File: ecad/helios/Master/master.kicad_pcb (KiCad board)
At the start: 2 copper layers, 100 x 100 mm, 129 parts, among them J1 MCV 1,5/ 3-G-3,5, J10 MiniFit JR 5556 08A2, J11 MCV 1,5/ 2-G-3,5, J12 MiniFit JR 5556 08A2, J13 M20-8760342, J2 MCV 1,5/ 2-G-3,5, J3 MCV 1,5/ 2-G-3,5, J4 MCV 1,5/ 2-G-3,5, J5 MCV 1,5/ 2-G-3,5, J6 MiniFit JR 5556 08A2, J7 MCV 1,5/ 2-G-3,5, J8 MiniFit JR 5556 08A2, J9 MCV 1,5/ 2-G-3,5, Q1 IRF9Z34NPbF, Q2 BSS84P, Q3 IRF9Z34NPbF, Q4 BSS84P, Q5 IRF9Z34NPbF, Q6 BSS84P, Q7 IRF9Z34NPbF, Q8 BSS84P, SW1 1825910-6, U1 NCP1117-5.0_SOT223, U10 ISO7320FC, U11 UA9638, U12 LM2842Y, U13 LP3985IM5-5.0/NOPB, U14 TPS1H100AQPWPRQ1, U15 ISO7320FC, U16 UA9638, U17 LM2842Y, U18 LP3985IM5-5.0/NOPB, U19 TPS1H100AQPWPRQ1, U2 MCP2561-E/SN, U20 ISO7320FC, U21 UA9638, U22 LM2842Y, U23 LP3985IM5-5.0/NOPB, U3 ATMEGA16M1-AU, U4 TPS1H100AQPWPRQ1, U5 ISO7320FC, U6 UA9638, U7 LM2842Y, U8 LP3985IM5-5.0/NOPB, U9 TPS1H100AQPWPRQ1, Y1 16MHz

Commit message: wip
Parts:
- added D14: 5.5V, FORT:D_0201, F.Cu at (127.5, 55.8)
- added D15: 5.5V, FORT:D_0201, F.Cu at (127.5, 54.2)
- added D16: 5.5V, FORT:D_0201, F.Cu at (127.5, 61.3)
- added D17: 5.5V, FORT:D_0201, F.Cu at (127.5, 59.7)
- added D18: 5.5V, FORT:D_0201, F.Cu at (177.5, 55.8)
- added D19: 5.5V, FORT:D_0201, F.Cu at (177.5, 54.2)
- added D20: 5.5V, FORT:D_0201, F.Cu at (177.5, 61.3)
- added D21: 5.5V, FORT:D_0201, F.Cu at (177.5, 59.7)
- added D22: 5.5V, FORT:D_0201, F.Cu at (152.5, 55.8)
- added D23: 5.5V, FORT:D_0201, F.Cu at (152.5, 54.2)
- added D24: 5.5V, FORT:D_0201, F.Cu at (152.5, 61.3)
- added D25: 5.5V, FORT:D_0201, F.Cu at (152.5, 59.7)
- added D26: 5.5V, FORT:D_0201, F.Cu at (102.5, 55.8)
- added D27: 5.5V, FORT:D_0201, F.Cu at (102.5, 54.2)
- added D28: 5.5V, FORT:D_0201, F.Cu at (102.7, 61.3)
- added D29: 5.5V, FORT:D_0201, F.Cu at (102.7, 59.7)
- added REF***: OSHW-Logo2_14.6x12mm_SilkScreen, Symbols:OSHW-Logo2_14.6x12mm_SilkScreen, F.Cu at (116.5, 129.8)
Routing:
- net /Output_3/PWRGND: track 344.8 -> 385.3 mm, vias 40 -> 45
- net /Output_1/PWRGND: track 360.4 -> 394.0 mm
- net /Output_4/PWRGND: track 349.1 -> 381.8 mm
- net +5V: track 291.4 -> 299.3 mm
- net (no net): track 6.00 -> 0.00 mm, vias 5 -> 0
- net /Output_3/DATA_-: track 62.3 -> 64.8 mm
- net /Output_1/IR_ON+: track 64.5 -> 66.2 mm
- net /Output_4/IR_ON+: track 64.5 -> 65.9 mm
- net /Output_3/IR_ON+: track 63.4 -> 64.8 mm
- net /Output_4/DATA_+: track 69.0 -> 70.4 mm
- net /Output_3/DATA_+: track 69.0 -> 70.4 mm
- net /Output_2/IR_ON+: track 63.7 -> 65.1 mm
- net /Output_1/IR_ON-: track 58.3 -> 59.6 mm
- net /Output_3/IR_ON-: track 57.7 -> 58.7 mm
- net /Output_4/IR_ON-: track 57.9 -> 59.0 mm
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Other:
- outline, holes or cut-outs redrawn
- net class Default: clearance 0.19 -> 0.175
- net class HighPower: clearance 0.19 -> 0.175
- net class LowPower: clearance 0.19 -> 0.175
- net class MidPower: clearance 0.19 -> 0.175
- rule trace_clearance: 0.19 -> 0.175
- board text added: "ICSP"
- board text added: "© 2018 Alexandre Tuleu HELIOS - Lighting Master Board"
- board text added: "•"

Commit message: wip
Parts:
- C13, C22, C31, C40: value 1uF -> 1uF, 50V
- C17, C26, C35, C44: value 0.01uF -> 10nF, 50V
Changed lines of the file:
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@@
     (pad_to_mask_clearance 0.08)
     (aux_axis_origin 102.5 128.7)
-    (grid_origin 100 150)
+    (grid_origin 102.5 128.7)
     (visible_elements FFFFFF7F)
     (pcbplotparams
@@
       (viasonmask false)
       (mode 1)
-      (useauxorigin false)
+      (useauxorigin true)
       (hpglpennumber 1)
       (hpglpenspeed 20)
@@
       (effects (font (size 1 1) (thickness 0.15)))
     )
-    (fp_text value 1uF (at 0 1.5 90) (layer F.Fab)
+    (fp_text value "1uF, 50V" (at 0 1.5 90) (layer F.Fab)
       (effects (font (size 1 1) (thickness 0.15)))
     )
@@
       (effects (font (size 1 1) (thickness 0.15)))
     )
-    (fp_text value 0.01uF (at 0 1.5 270) (layer F.Fab)
+    (fp_text value "10nF, 50V" (at 0 1.5 270) (layer F.Fab)
       (effects (font (size 1 1) (thickness 0.15)))
     )
@@
     (tags "capacitor 0603")
     (attr smd)
-    (fp_text reference C22 (at 0 -1.5 90) (layer F.SilkS)
+    (fp_text reference C22 (at 0 2.2 180) (layer F.SilkS)
       (effects (font (size 1 1) (thickness 0.15)))
     )
-    (fp_text value 1uF (at 0 1.5 90) (layer F.Fab)
+    (fp_text value "1uF, 50V" (at 0 1.5 90) (layer F.Fab)
       (effects (font (size 1 1) (thickness 0.15)))
     )
@@
     (tags "capacitor 1206")
     (attr smd)
-    (fp_text reference C24 (at 0 -1.75) (layer F.SilkS)
+    (fp_text reference C24 (at 3.6 0) (layer F.SilkS)
       (effects (font (size 1 1) (thickness 0.15)))
     )
@@
       (effects (font (size 1 1) (thickness 0.15)))
     )
-    (fp_text value 0.01uF (at 0 1.5 270) (layer F.Fab)
+    (fp_text value "10nF, 50V" (at 0 1.5 270) (layer F.Fab)
       (effects (font (size 1 1) (thickness 0.15)))
     )
@@
       (effects (font (size 1 1) (thickness 0.15)))
     )
-    (fp_text value 1uF (at 0 1.5 90) (layer F.Fab)
+    (fp_text value "1uF, 50V" (at 0 1.5 90) (layer F.Fab)
       (effects (font (size 1 1) (thickness 0.15)))
     )
@@
       (effects (font (size 1 1) (thickness 0.15)))
     )
-    (fp_text value 0.01uF (at 0 1.5 270) (layer F.Fab)
+    (fp_text value "10nF, 50V" (at 0 1.5 270) (layer F.Fab)
       (effects (font (size 1 1) (thickness 0.15)))
     )
@@
       (effects (font (size 1 1) (thickness 0.15)))
     )
-    (fp_text value 1uF (at 0 1.5 90) (layer F.Fab)
+    (fp_text value "1uF, 50V" (at 0 1.5 90) (layer F.Fab)
       (effects (font (size 1 1) (thickness 0.15)))
     )
@@
       (effects (font (size 1 1) (thickness 0.15)))
     )
-    (fp_text value 0.01uF (at 0 1.5 270) (layer F.Fab)
+    (fp_text value "10nF, 50V" (at 0 1.5 270) (layer F.Fab)
       (effects (font (size 1 1) (thickness 0.15)))
     )
@@
     (tags SOD-123)
     (attr smd)
-    (fp_text reference D6 (at 0 -2 90) (layer F.SilkS)
+    (fp_text reference D6 (at 2.9 0 180) (layer F.SilkS)
       (effects (font (size 1 1) (thickness 0.15)))
     )
@@
     (at 133.8 71.8 180)
     (attr smd)
-    (fp_text reference L1 (at -3.4 6.3 180) (layer F.SilkS)
+    (fp_text reference L1 (at 4.7 6.3 180) (layer F.SilkS)
       (effects (font (size 1 1) (thickness 0.15)))
     )
@@
     (at 108.8 71.8 180)
     (attr smd)
-    (fp_text reference L4 (at -3.4 6.3 180) (layer F.SilkS)
+    (fp_text reference L4 (at 4.7 6.3 180) (layer F.SilkS)
       (effects (font (size 1 1) (thickness 0.15)))
     )
@@
     (at 158.8 71.8 180)
     (attr smd)
-    (fp_text reference L3 (at -3.4 6.3 180) (layer F.SilkS)
+    (fp_text reference L3 (at 4.7 6.3 180) (layer F.SilkS)
       (effects (font (size 1 1) (thickness 0.15)))
     )
@@
     (at 183.8 71.8 180)
     (attr smd)
-    (fp_text reference L2 (at -3.4 6.3 180) (layer F.SilkS)
+    (fp_text reference L2 (at 4.7 6.4 180) (layer F.SilkS)
       (effects (font (size 1 1) (thickness 0.15)))
     )

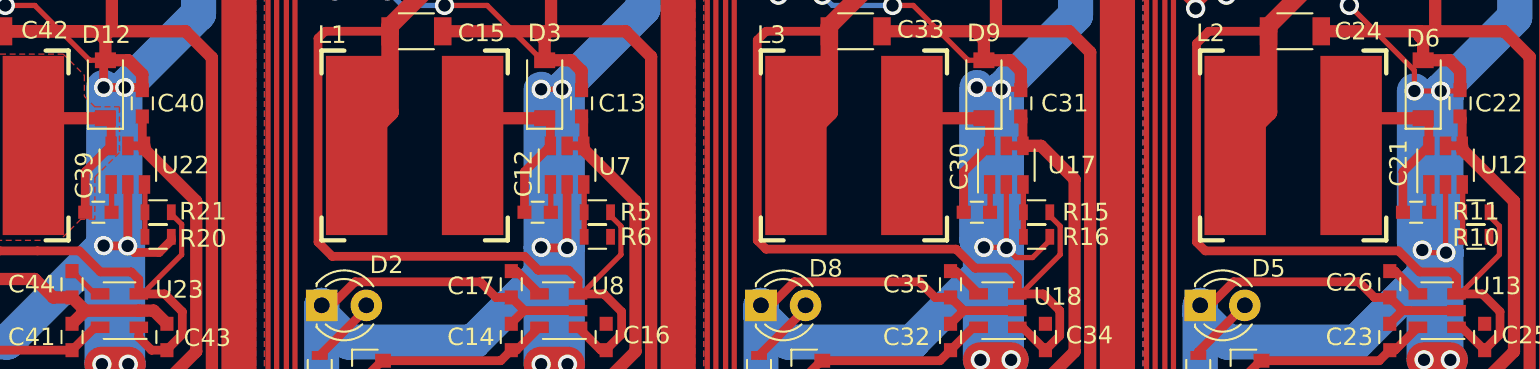
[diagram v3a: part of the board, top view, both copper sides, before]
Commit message: Adds step exports of all boards
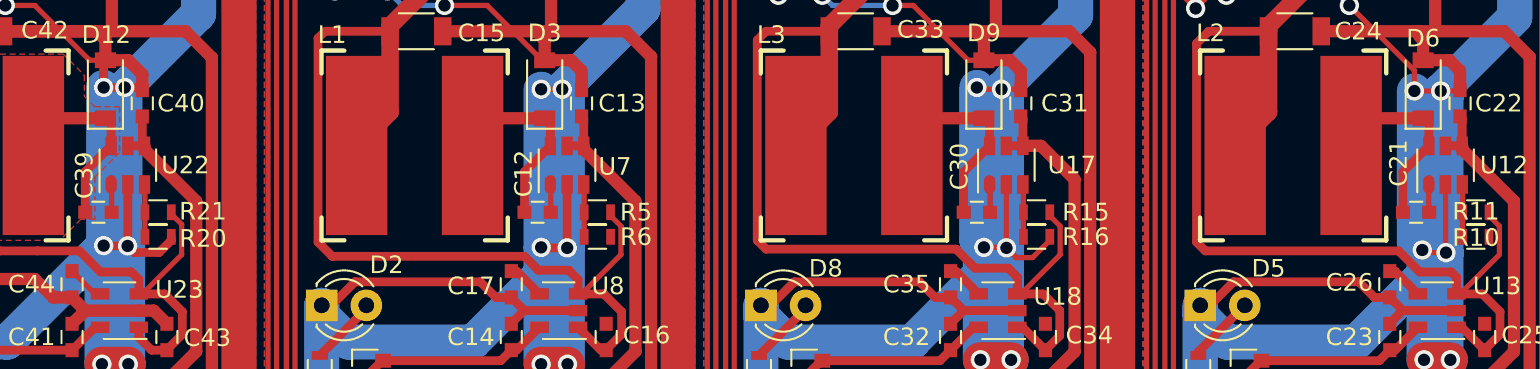
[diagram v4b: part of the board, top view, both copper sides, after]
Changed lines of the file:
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@@
     (links 394)
     (no_connects 0)
-    (area 98.55 49.924999 200.805952 150.075001)
+    (area 99.924999 49.924999 200.075001 150.075001)
     (thickness 1.6)
     (drawings 15)
@@
     (mod_text_size 1 1)
     (mod_text_width 0.15)
-    (pad_size 1.524 1.524)
-    (pad_drill 0.762)
+    (pad_size 1.06 0.65)
+    (pad_drill 0)
     (pad_to_mask_clearance 0.08)
     (aux_axis_origin 102.5 128.7)
@@
     (fp_line (start 0.9 1.55) (end -0.9 1.55) (layer F.Fab) (width 0.1))
     (fp_line (start 0.9 -1.55) (end 0.9 1.55) (layer F.Fab) (width 0.1))
-    (pad 1 smd rect (at -1.1 -0.95 90) (size 1.06 0.65) (layers F.Cu F.Paste F.Mask)
+    (pad 1 smd oval (at -1.1 -0.95 90) (size 1.06 0.65) (layers F.Cu F.Paste F.Mask)
       (net 45 /Output_2/6V_Regulator/BOOT))
     (pad 2 smd rect (at -1.1 0 90) (size 1.06 0.65) (layers F.Cu F.Paste F.Mask)
@@
     (fp_line (start 0.9 1.55) (end -0.9 1.55) (layer F.Fab) (width 0.1))
     (fp_line (start 0.9 -1.55) (end 0.9 1.55) (layer F.Fab) (width 0.1))
-    (pad 1 smd rect (at -1.1 -0.95 90) (size 1.06 0.65) (layers F.Cu F.Paste F.Mask)
+    (pad 1 smd oval (at -1.1 -0.95 90) (size 1.06 0.65) (layers F.Cu F.Paste F.Mask)
       (net 49 /Output_3/6V_Regulator/BOOT))
     (pad 2 smd rect (at -1.1 0 90) (size 1.06 0.65) (layers F.Cu F.Paste F.Mask)
@@
     (fp_line (start 0.9 1.55) (end -0.9 1.55) (layer F.Fab) (width 0.1))
     (fp_line (start 0.9 -1.55) (end 0.9 1.55) (layer F.Fab) (width 0.1))
-    (pad 1 smd rect (at -1.1 -0.95 90) (size 1.06 0.65) (layers F.Cu F.Paste F.Mask)
+    (pad 1 smd oval (at -1.1 -0.95 90) (size 1.06 0.65) (layers F.Cu F.Paste F.Mask)
       (net 53 /Output_4/6V_Regulator/BOOT))
     (pad 2 smd rect (at -1.1 0 90) (size 1.06 0.65) (layers F.Cu F.Paste F.Mask)
@@
     (fp_line (start 0.9 1.55) (end -0.9 1.55) (layer F.Fab) (width 0.1))
     (fp_line (start 0.9 -1.55) (end 0.9 1.55) (layer F.Fab) (width 0.1))
-    (pad 1 smd rect (at -1.1 -0.95 90) (size 1.06 0.65) (layers F.Cu F.Paste F.Mask)
+    (pad 1 smd oval (at -1.1 -0.95 90) (size 1.06 0.65) (layers F.Cu F.Paste F.Mask)
       (net 57 /Output_1/6V_Regulator/BOOT))
     (pad 2 smd rect (at -1.1 0 90) (size 1.06 0.65) (layers F.Cu F.Paste F.Mask)

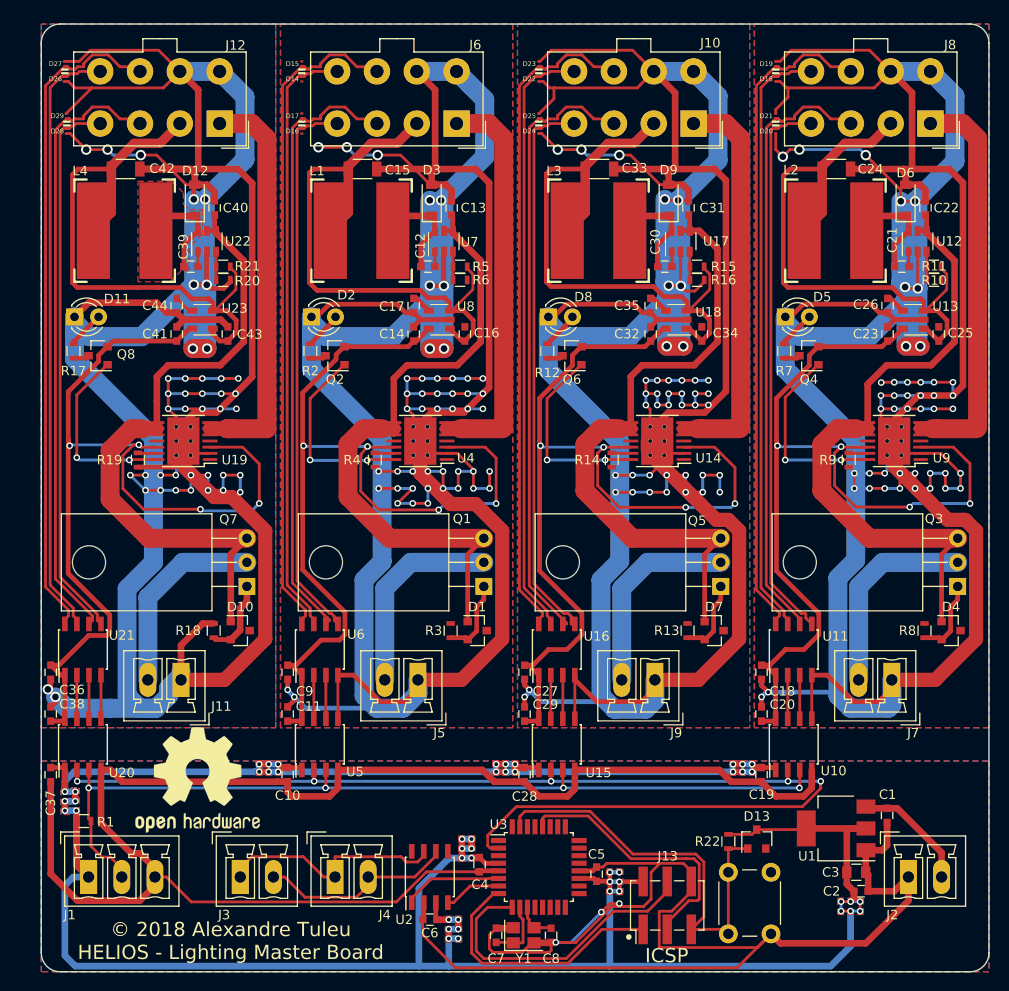
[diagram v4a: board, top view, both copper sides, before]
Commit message: Uses STEF01 instead of TPS1H100
The later makes everything explode on shortcut.

The former works nicely.
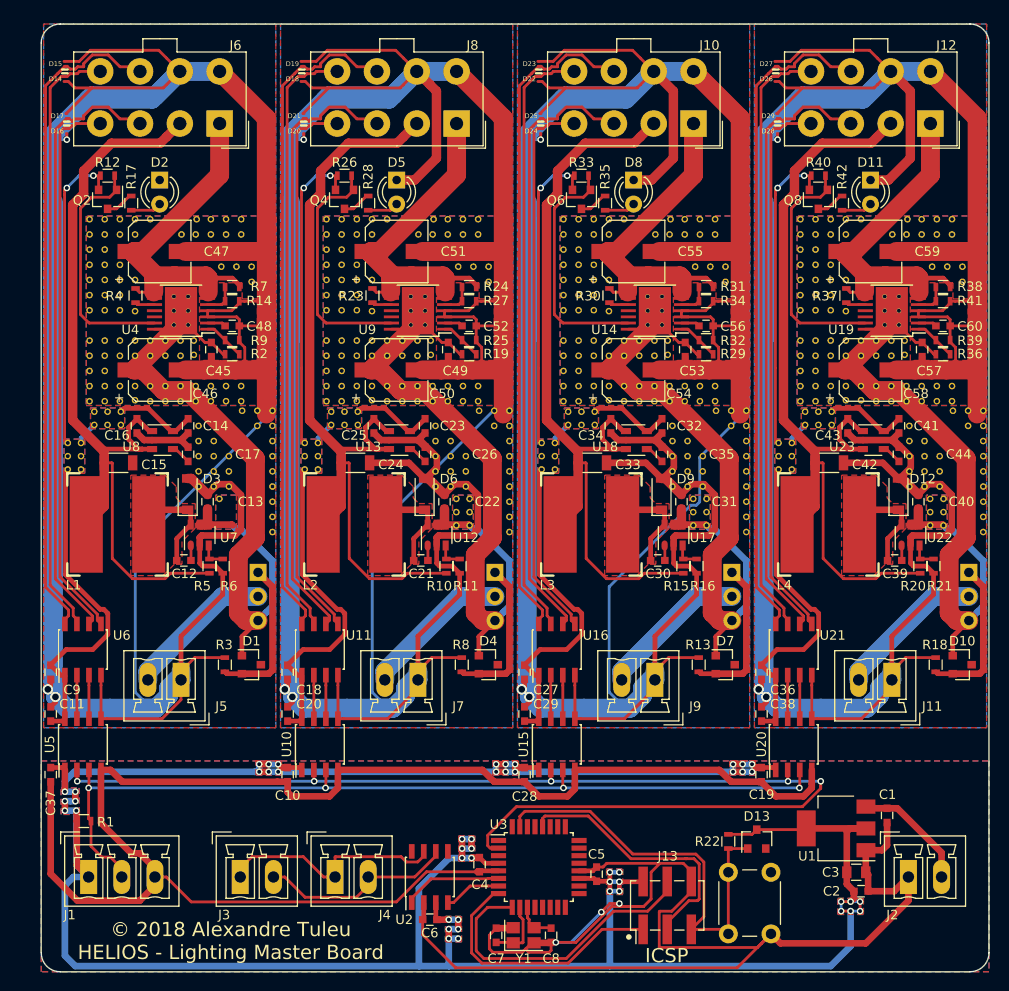
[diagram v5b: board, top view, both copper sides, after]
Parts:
- removed REF***: OSHW-Logo2_14.6x12mm_SilkScreen, Symbols:OSHW-Logo2_14.6x12mm_SilkScreen
- added C45: 100nF, Capacitors_SMD:C_0603, F.Cu at (118.0, 84.3)
- added C46: 47uF, 50V, Capacitors_SMD:CP_Elec_6.3x7.7, F.Cu at (112.5, 86.5)
- added C47: 47uF, 50V, Capacitors_SMD:CP_Elec_6.3x7.7, F.Cu at (112.5, 74.0)
- added C48: 10nF, 50V, Capacitors_SMD:C_0603, F.Cu at (120.2, 81.8)
- added C49: 100nF, Capacitors_SMD:C_0603, F.Cu at (142.9, 84.3)
- added C50: 47uF, 50V, Capacitors_SMD:CP_Elec_6.3x7.7, F.Cu at (137.5, 86.5)
- added C51: 47uF, 50V, Capacitors_SMD:CP_Elec_6.3x7.7, F.Cu at (137.5, 74.0)
- added C52: 10nF, 50V, Capacitors_SMD:C_0603, F.Cu at (145.2, 81.8)
- added C53: 100nF, Capacitors_SMD:C_0603, F.Cu at (167.9, 84.3)
- added C54: 47uF, 50V, Capacitors_SMD:CP_Elec_6.3x7.7, F.Cu at (162.5, 86.5)
- added C55: 47uF, 50V, Capacitors_SMD:CP_Elec_6.3x7.7, F.Cu at (162.5, 74.0)
- added C56: 10nF, 50V, Capacitors_SMD:C_0603, F.Cu at (170.2, 81.8)
- added C57: 100nF, Capacitors_SMD:C_0603, F.Cu at (192.9, 84.3)
- added C58: 47uF, 50V, Capacitors_SMD:CP_Elec_6.3x7.7, F.Cu at (187.5, 86.5)
- added C59: 47uF, 50V, Capacitors_SMD:CP_Elec_6.3x7.7, F.Cu at (187.5, 74.0)
- added C60: 10nF, 50V, Capacitors_SMD:C_0603, F.Cu at (195.2, 81.8)
- added R23: 25.5, Resistors_SMD:R_0603, F.Cu at (134.9, 78.7)
- added R24: 301K, Resistors_SMD:R_0603, F.Cu at (145.2, 77.8)
- added R25: 10K, Resistors_SMD:R_0603, F.Cu at (145.2, 83.3)
- added R26: 100K, Resistors_SMD:R_0603, F.Cu at (132.0, 66.0)
- added R27: 10K, Resistors_SMD:R_0603, F.Cu at (145.2, 79.2)
- added R28: 604, Resistors_SMD:R_0603, F.Cu at (134.5, 68.9)
- added R29: 249K, Resistors_SMD:R_0603, F.Cu at (170.2, 84.8)
- added R30: 25.5, Resistors_SMD:R_0603, F.Cu at (159.9, 78.7)
- added R31: 301K, Resistors_SMD:R_0603, F.Cu at (170.2, 77.8)
- added R32: 10K, Resistors_SMD:R_0603, F.Cu at (170.2, 83.3)
- added R33: 100K, Resistors_SMD:R_0603, F.Cu at (157.0, 66.0)
- added R34: 10K, Resistors_SMD:R_0603, F.Cu at (170.2, 79.2)
- added R35: 604, Resistors_SMD:R_0603, F.Cu at (159.5, 68.9)
- added R36: 249K, Resistors_SMD:R_0603, F.Cu at (195.2, 84.8)
- added R37: 25.5, Resistors_SMD:R_0603, F.Cu at (184.9, 78.7)
- added R38: 301K, Resistors_SMD:R_0603, F.Cu at (195.2, 77.8)
- added R39: 10K, Resistors_SMD:R_0603, F.Cu at (195.2, 83.3)
- added R40: 100K, Resistors_SMD:R_0603, F.Cu at (182.0, 66.0)
- added R41: 10K, Resistors_SMD:R_0603, F.Cu at (195.2, 79.2)
- added R42: 604, Resistors_SMD:R_0603, F.Cu at (184.5, 68.9)
- added REF**: VIA_0.7mm, VIA_0.7mm, F.Cu at (119.8, 98.8)
- added REF**: VIA_0.7mm, VIA_0.7mm, F.Cu at (118.2, 94.0)
- added REF**: VIA_0.7mm, VIA_0.7mm, F.Cu at (159.9, 88.2)
- added REF**: VIA_0.7mm, VIA_0.7mm, F.Cu at (158.3, 88.2)
- added REF**: VIA_0.7mm, VIA_0.7mm, F.Cu at (156.7, 88.2)
- added REF**: VIA_0.7mm, VIA_0.7mm, F.Cu at (121.1, 88.2)
- added REF**: VIA_0.7mm, VIA_0.7mm, F.Cu at (119.5, 88.2)
- added REF**: VIA_0.7mm, VIA_0.7mm, F.Cu at (117.9, 88.2)
- added REF**: VIA_0.7mm, VIA_0.7mm, F.Cu at (116.3, 88.2)
- added REF**: VIA_0.7mm, VIA_0.7mm, F.Cu at (114.7, 88.2)
- added REF**: VIA_0.7mm, VIA_0.7mm, F.Cu at (113.1, 88.2)
- added REF**: VIA_0.7mm, VIA_0.7mm, F.Cu at (111.5, 88.2)
- added REF**: VIA_0.7mm, VIA_0.7mm, F.Cu at (116.6, 94.0)
- added REF**: VIA_0.7mm, VIA_0.7mm, F.Cu at (109.9, 88.2)
- added REF**: VIA_0.7mm, VIA_0.7mm, F.Cu at (108.3, 88.2)
- added REF**: VIA_0.7mm, VIA_0.7mm, F.Cu at (106.7, 88.2)
- added REF**: VIA_0.7mm, VIA_0.7mm, F.Cu at (146.1, 89.8)
- added REF**: VIA_0.7mm, VIA_0.7mm, F.Cu at (144.5, 89.8)
- added REF**: VIA_0.7mm, VIA_0.7mm, F.Cu at (142.9, 89.8)
- added REF**: VIA_0.7mm, VIA_0.7mm, F.Cu at (141.3, 89.8)
- added REF**: VIA_0.7mm, VIA_0.7mm, F.Cu at (139.7, 89.8)
- added REF**: VIA_0.7mm, VIA_0.7mm, F.Cu at (138.1, 89.8)
- added REF**: VIA_0.7mm, VIA_0.7mm, F.Cu at (136.5, 89.8)
- added REF**: VIA_0.7mm, VIA_0.7mm, F.Cu at (169.8, 98.8)
- added REF**: VIA_0.7mm, VIA_0.7mm, F.Cu at (134.9, 89.7)
- added REF**: VIA_0.7mm, VIA_0.7mm, F.Cu at (133.3, 89.8)
- added REF**: VIA_0.7mm, VIA_0.7mm, F.Cu at (131.7, 89.8)
- added REF**: VIA_0.7mm, VIA_0.7mm, F.Cu at (146.1, 88.2)
- added REF**: VIA_0.7mm, VIA_0.7mm, F.Cu at (144.5, 88.2)
- added REF**: VIA_0.7mm, VIA_0.7mm, F.Cu at (142.9, 88.2)
- added REF**: VIA_0.7mm, VIA_0.7mm, F.Cu at (141.3, 88.2)
- added REF**: VIA_0.7mm, VIA_0.7mm, F.Cu at (139.7, 88.2)
- added REF**: VIA_0.7mm, VIA_0.7mm, F.Cu at (138.1, 88.2)
- added REF**: VIA_0.7mm, VIA_0.7mm, F.Cu at (136.5, 88.2)
- added REF**: VIA_0.7mm, VIA_0.7mm, F.Cu at (168.2, 98.8)
- added REF**: VIA_0.7mm, VIA_0.7mm, F.Cu at (134.9, 88.2)
- added REF**: VIA_0.7mm, VIA_0.7mm, F.Cu at (133.3, 88.2)
- added REF**: VIA_0.7mm, VIA_0.7mm, F.Cu at (131.7, 88.2)
- added REF**: VIA_0.7mm, VIA_0.7mm, F.Cu at (156.7, 86.6)
- added REF**: VIA_0.7mm, VIA_0.7mm, F.Cu at (106.7, 86.6)
- added REF**: VIA_0.7mm, VIA_0.7mm, F.Cu at (131.7, 86.6)
- added REF**: VIA_0.7mm, VIA_0.7mm, F.Cu at (141.1, 83.4)
- added REF**: VIA_0.7mm, VIA_0.7mm, F.Cu at (139.7, 83.4)
- added REF**: VIA_0.7mm, VIA_0.7mm, F.Cu at (138.1, 83.4)
- added REF**: VIA_0.7mm, VIA_0.7mm, F.Cu at (136.5, 83.4)
- added REF**: VIA_0.7mm, VIA_0.7mm, F.Cu at (166.6, 98.8)
- added REF**: VIA_0.7mm, VIA_0.7mm, F.Cu at (134.9, 83.4)
- added REF**: VIA_0.7mm, VIA_0.7mm, F.Cu at (133.3, 83.4)
- added REF**: VIA_0.7mm, VIA_0.7mm, F.Cu at (131.7, 83.4)
- added REF**: VIA_0.7mm, VIA_0.7mm, F.Cu at (116.1, 84.9)
- added REF**: VIA_0.7mm, VIA_0.7mm, F.Cu at (114.7, 85.0)
- added REF**: VIA_0.7mm, VIA_0.7mm, F.Cu at (113.1, 85.0)
- added REF**: VIA_0.7mm, VIA_0.7mm, F.Cu at (111.5, 85.0)
- added REF**: VIA_0.7mm, VIA_0.7mm, F.Cu at (109.9, 85.0)
- added REF**: VIA_0.7mm, VIA_0.7mm, F.Cu at (108.3, 85.0)
- added REF**: VIA_0.7mm, VIA_0.7mm, F.Cu at (106.7, 85.0)
- added REF**: VIA_0.7mm, VIA_0.7mm, F.Cu at (169.8, 97.2)
- added REF**: VIA_0.7mm, VIA_0.7mm, F.Cu at (166.1, 84.9)
- added REF**: VIA_0.7mm, VIA_0.7mm, F.Cu at (164.7, 85.0)
- added REF**: VIA_0.7mm, VIA_0.7mm, F.Cu at (163.1, 85.0)
- added REF**: VIA_0.7mm, VIA_0.7mm, F.Cu at (161.5, 85.0)
- added REF**: VIA_0.7mm, VIA_0.7mm, F.Cu at (159.9, 85.0)
- added REF**: VIA_0.7mm, VIA_0.7mm, F.Cu at (158.3, 85.0)
- added REF**: VIA_0.7mm, VIA_0.7mm, F.Cu at (156.7, 85.0)
- added REF**: VIA_0.7mm, VIA_0.7mm, F.Cu at (166.1, 83.4)
- added REF**: VIA_0.7mm, VIA_0.7mm, F.Cu at (164.7, 83.4)
- added REF**: VIA_0.7mm, VIA_0.7mm, F.Cu at (163.1, 83.4)
- added REF**: VIA_0.7mm, VIA_0.7mm, F.Cu at (168.2, 97.2)
- added REF**: VIA_0.7mm, VIA_0.7mm, F.Cu at (161.5, 83.4)
- added REF**: VIA_0.7mm, VIA_0.7mm, F.Cu at (159.9, 83.4)
- added REF**: VIA_0.7mm, VIA_0.7mm, F.Cu at (158.3, 83.4)
- added REF**: VIA_0.7mm, VIA_0.7mm, F.Cu at (156.7, 83.4)
- added REF**: VIA_0.7mm, VIA_0.7mm, F.Cu at (116.1, 83.4)
- added REF**: VIA_0.7mm, VIA_0.7mm, F.Cu at (114.7, 83.4)
- added REF**: VIA_0.7mm, VIA_0.7mm, F.Cu at (113.1, 83.4)
- added REF**: VIA_0.7mm, VIA_0.7mm, F.Cu at (111.5, 83.4)
- added REF**: VIA_0.7mm, VIA_0.7mm, F.Cu at (109.9, 83.4)
- added REF**: VIA_0.7mm, VIA_0.7mm, F.Cu at (108.3, 83.4)
- added REF**: VIA_0.7mm, VIA_0.7mm, F.Cu at (166.6, 97.2)
- added REF**: VIA_0.7mm, VIA_0.7mm, F.Cu at (106.7, 83.4)
- added REF**: VIA_0.7mm, VIA_0.7mm, F.Cu at (141.1, 84.9)
- added REF**: VIA_0.7mm, VIA_0.7mm, F.Cu at (139.7, 85.0)
- added REF**: VIA_0.7mm, VIA_0.7mm, F.Cu at (138.1, 85.0)
- added REF**: VIA_0.7mm, VIA_0.7mm, F.Cu at (136.5, 85.0)
- added REF**: VIA_0.7mm, VIA_0.7mm, F.Cu at (134.9, 85.0)
- added REF**: VIA_0.7mm, VIA_0.7mm, F.Cu at (133.3, 85.0)
- added REF**: VIA_0.7mm, VIA_0.7mm, F.Cu at (131.7, 85.0)
- added REF**: VIA_0.7mm, VIA_0.7mm, F.Cu at (155.1, 89.8)
- added REF**: VIA_0.7mm, VIA_0.7mm, F.Cu at (155.1, 88.2)
- added REF**: VIA_0.7mm, VIA_0.7mm, F.Cu at (169.8, 95.6)
- added REF**: VIA_0.7mm, VIA_0.7mm, F.Cu at (155.1, 86.6)
- added REF**: VIA_0.7mm, VIA_0.7mm, F.Cu at (155.1, 85.0)
- added REF**: VIA_0.7mm, VIA_0.7mm, F.Cu at (155.1, 83.4)
- added REF**: VIA_0.7mm, VIA_0.7mm, F.Cu at (130.1, 89.8)
- added REF**: VIA_0.7mm, VIA_0.7mm, F.Cu at (130.1, 88.2)
- added REF**: VIA_0.7mm, VIA_0.7mm, F.Cu at (130.1, 86.6)
- added REF**: VIA_0.7mm, VIA_0.7mm, F.Cu at (130.1, 85.0)
- added REF**: VIA_0.7mm, VIA_0.7mm, F.Cu at (130.1, 83.4)
- added REF**: VIA_0.7mm, VIA_0.7mm, F.Cu at (105.1, 89.8)
- added REF**: VIA_0.7mm, VIA_0.7mm, F.Cu at (105.1, 88.2)
- added REF**: VIA_0.7mm, VIA_0.7mm, F.Cu at (168.2, 95.6)
- added REF**: VIA_0.7mm, VIA_0.7mm, F.Cu at (105.1, 86.6)
- added REF**: VIA_0.7mm, VIA_0.7mm, F.Cu at (105.1, 85.0)
- added REF**: VIA_0.7mm, VIA_0.7mm, F.Cu at (105.1, 83.4)
- added REF**: VIA_0.7mm, VIA_0.7mm, F.Cu at (147.2, 77.2)
- added REF**: VIA_0.7mm, VIA_0.7mm, F.Cu at (147.2, 75.6)
- added REF**: VIA_0.7mm, VIA_0.7mm, F.Cu at (145.6, 75.6)
- added REF**: VIA_0.7mm, VIA_0.7mm, F.Cu at (172.2, 77.2)
- added REF**: VIA_0.7mm, VIA_0.7mm, F.Cu at (172.2, 75.6)
- added REF**: VIA_0.7mm, VIA_0.7mm, F.Cu at (170.6, 75.6)
- added REF**: VIA_0.7mm, VIA_0.7mm, F.Cu at (122.2, 77.2)
- added REF**: VIA_0.7mm, VIA_0.7mm, F.Cu at (118.2, 98.8)
- added REF**: VIA_0.7mm, VIA_0.7mm, F.Cu at (166.6, 95.6)
- added REF**: VIA_0.7mm, VIA_0.7mm, F.Cu at (122.2, 75.6)
- added REF**: VIA_0.7mm, VIA_0.7mm, F.Cu at (120.6, 75.6)
- added REF**: VIA_0.7mm, VIA_0.7mm, F.Cu at (197.2, 75.6)
- added REF**: VIA_0.7mm, VIA_0.7mm, F.Cu at (169.0, 75.6)
- added REF**: VIA_0.7mm, VIA_0.7mm, F.Cu at (144.0, 75.6)
- added REF**: VIA_0.7mm, VIA_0.7mm, F.Cu at (106.7, 73.8)
- added REF**: VIA_0.7mm, VIA_0.7mm, F.Cu at (131.7, 73.8)
- added REF**: VIA_0.7mm, VIA_0.7mm, F.Cu at (109.9, 77.0)
- added REF**: VIA_0.7mm, VIA_0.7mm, F.Cu at (108.3, 77.0)
- added REF**: VIA_0.7mm, VIA_0.7mm, F.Cu at (106.7, 77.0)
- added REF**: VIA_0.7mm, VIA_0.7mm, F.Cu at (168.2, 94.0)
- added REF**: VIA_0.7mm, VIA_0.7mm, F.Cu at (133.3, 78.6)
- added REF**: VIA_0.7mm, VIA_0.7mm, F.Cu at (131.7, 78.6)
- added REF**: VIA_0.7mm, VIA_0.7mm, F.Cu at (109.9, 80.3)
- added REF**: VIA_0.7mm, VIA_0.7mm, F.Cu at (108.3, 80.2)
- added REF**: VIA_0.7mm, VIA_0.7mm, F.Cu at (106.7, 80.2)
- added REF**: VIA_0.7mm, VIA_0.7mm, F.Cu at (158.3, 75.4)
- added REF**: VIA_0.7mm, VIA_0.7mm, F.Cu at (156.7, 75.4)
- added REF**: VIA_0.7mm, VIA_0.7mm, F.Cu at (133.3, 75.4)
- added REF**: VIA_0.7mm, VIA_0.7mm, F.Cu at (131.7, 75.4)
- added REF**: VIA_0.7mm, VIA_0.7mm, F.Cu at (134.9, 80.3)
- added REF**: VIA_0.7mm, VIA_0.7mm, F.Cu at (166.6, 94.0)
- added REF**: VIA_0.7mm, VIA_0.7mm, F.Cu at (133.3, 80.2)
- added REF**: VIA_0.7mm, VIA_0.7mm, F.Cu at (131.7, 80.2)
- added REF**: VIA_0.7mm, VIA_0.7mm, F.Cu at (159.9, 80.3)
- added REF**: VIA_0.7mm, VIA_0.7mm, F.Cu at (158.3, 80.2)
- added REF**: VIA_0.7mm, VIA_0.7mm, F.Cu at (156.7, 80.2)
- added REF**: VIA_0.7mm, VIA_0.7mm, F.Cu at (158.3, 78.6)
- added REF**: VIA_0.7mm, VIA_0.7mm, F.Cu at (156.7, 78.6)
- added REF**: VIA_0.7mm, VIA_0.7mm, F.Cu at (108.3, 78.6)
- added REF**: VIA_0.7mm, VIA_0.7mm, F.Cu at (106.7, 78.6)
- added REF**: VIA_0.7mm, VIA_0.7mm, F.Cu at (108.3, 75.4)
- added REF**: VIA_0.7mm, VIA_0.7mm, F.Cu at (144.8, 98.8)
- added REF**: VIA_0.7mm, VIA_0.7mm, F.Cu at (106.7, 75.4)
- added REF**: VIA_0.7mm, VIA_0.7mm, F.Cu at (134.9, 77.0)
- added REF**: VIA_0.7mm, VIA_0.7mm, F.Cu at (133.3, 77.0)
- added REF**: VIA_0.7mm, VIA_0.7mm, F.Cu at (131.7, 77.0)
- added REF**: VIA_0.7mm, VIA_0.7mm, F.Cu at (159.9, 77.0)
- added REF**: VIA_0.7mm, VIA_0.7mm, F.Cu at (158.3, 77.0)
- added REF**: VIA_0.7mm, VIA_0.7mm, F.Cu at (156.7, 77.0)
- added REF**: VIA_0.7mm, VIA_0.7mm, F.Cu at (156.7, 73.8)
- added REF**: VIA_0.7mm, VIA_0.7mm, F.Cu at (146.1, 72.2)
- added REF**: VIA_0.7mm, VIA_0.7mm, F.Cu at (144.5, 72.2)
- added REF**: VIA_0.7mm, VIA_0.7mm, F.Cu at (143.2, 98.8)
- added REF**: VIA_0.7mm, VIA_0.7mm, F.Cu at (142.9, 72.2)
- added REF**: VIA_0.7mm, VIA_0.7mm, F.Cu at (141.3, 72.2)
- added REF**: VIA_0.7mm, VIA_0.7mm, F.Cu at (139.8, 72.2)
- added REF**: VIA_0.7mm, VIA_0.7mm, F.Cu at (134.9, 72.2)
- added REF**: VIA_0.7mm, VIA_0.7mm, F.Cu at (133.3, 72.2)
- added REF**: VIA_0.7mm, VIA_0.7mm, F.Cu at (131.7, 72.2)
- added REF**: VIA_0.7mm, VIA_0.7mm, F.Cu at (146.1, 70.6)
- added REF**: VIA_0.7mm, VIA_0.7mm, F.Cu at (144.5, 70.6)
- added REF**: VIA_0.7mm, VIA_0.7mm, F.Cu at (142.9, 70.6)
- added REF**: VIA_0.7mm, VIA_0.7mm, F.Cu at (141.4, 70.6)
- added REF**: VIA_0.7mm, VIA_0.7mm, F.Cu at (141.6, 98.8)
- added REF**: VIA_0.7mm, VIA_0.7mm, F.Cu at (136.5, 70.6)
- added REF**: VIA_0.7mm, VIA_0.7mm, F.Cu at (134.9, 70.6)
- added REF**: VIA_0.7mm, VIA_0.7mm, F.Cu at (133.3, 70.6)
- added REF**: VIA_0.7mm, VIA_0.7mm, F.Cu at (131.7, 70.6)
- added REF**: VIA_0.7mm, VIA_0.7mm, F.Cu at (121.1, 72.2)
- added REF**: VIA_0.7mm, VIA_0.7mm, F.Cu at (119.5, 72.2)
- added REF**: VIA_0.7mm, VIA_0.7mm, F.Cu at (117.9, 72.2)
- added REF**: VIA_0.7mm, VIA_0.7mm, F.Cu at (116.3, 72.2)
- added REF**: VIA_0.7mm, VIA_0.7mm, F.Cu at (114.8, 72.2)
- added REF**: VIA_0.7mm, VIA_0.7mm, F.Cu at (109.9, 72.2)
- added REF**: VIA_0.7mm, VIA_0.7mm, F.Cu at (144.8, 97.2)
- added REF**: VIA_0.7mm, VIA_0.7mm, F.Cu at (108.3, 72.2)
- added REF**: VIA_0.7mm, VIA_0.7mm, F.Cu at (106.7, 72.2)
- added REF**: VIA_0.7mm, VIA_0.7mm, F.Cu at (121.1, 70.6)
- added REF**: VIA_0.7mm, VIA_0.7mm, F.Cu at (119.5, 70.6)
- added REF**: VIA_0.7mm, VIA_0.7mm, F.Cu at (117.9, 70.6)
- added REF**: VIA_0.7mm, VIA_0.7mm, F.Cu at (116.4, 70.6)
- added REF**: VIA_0.7mm, VIA_0.7mm, F.Cu at (111.5, 70.6)
- added REF**: VIA_0.7mm, VIA_0.7mm, F.Cu at (109.9, 70.6)
- added REF**: VIA_0.7mm, VIA_0.7mm, F.Cu at (108.3, 70.6)
- added REF**: VIA_0.7mm, VIA_0.7mm, F.Cu at (106.7, 70.6)
- added REF**: VIA_0.7mm, VIA_0.7mm, F.Cu at (143.2, 97.2)
- added REF**: VIA_0.7mm, VIA_0.7mm, F.Cu at (155.1, 72.2)
- added REF**: VIA_0.7mm, VIA_0.7mm, F.Cu at (155.1, 70.6)
- added REF**: VIA_0.7mm, VIA_0.7mm, F.Cu at (171.1, 70.6)
- added REF**: VIA_0.7mm, VIA_0.7mm, F.Cu at (169.5, 70.6)
- added REF**: VIA_0.7mm, VIA_0.7mm, F.Cu at (167.9, 70.6)
- added REF**: VIA_0.7mm, VIA_0.7mm, F.Cu at (166.4, 70.6)
- added REF**: VIA_0.7mm, VIA_0.7mm, F.Cu at (161.5, 70.6)
- added REF**: VIA_0.7mm, VIA_0.7mm, F.Cu at (159.9, 70.6)
- added REF**: VIA_0.7mm, VIA_0.7mm, F.Cu at (158.3, 70.6)
- added REF**: VIA_0.7mm, VIA_0.7mm, F.Cu at (156.7, 70.6)
- added REF**: VIA_0.7mm, VIA_0.7mm, F.Cu at (141.6, 97.2)
- added REF**: VIA_0.7mm, VIA_0.7mm, F.Cu at (171.1, 72.2)
- added REF**: VIA_0.7mm, VIA_0.7mm, F.Cu at (169.5, 72.2)
- added REF**: VIA_0.7mm, VIA_0.7mm, F.Cu at (167.9, 72.2)
- added REF**: VIA_0.7mm, VIA_0.7mm, F.Cu at (166.3, 72.2)
- added REF**: VIA_0.7mm, VIA_0.7mm, F.Cu at (164.8, 72.2)
- added REF**: VIA_0.7mm, VIA_0.7mm, F.Cu at (159.9, 72.2)
- added REF**: VIA_0.7mm, VIA_0.7mm, F.Cu at (158.3, 72.2)
- added REF**: VIA_0.7mm, VIA_0.7mm, F.Cu at (156.7, 72.2)
- added REF**: VIA_0.7mm, VIA_0.7mm, F.Cu at (130.1, 80.2)
- added REF**: VIA_0.7mm, VIA_0.7mm, F.Cu at (130.1, 78.6)
- added REF**: VIA_0.7mm, VIA_0.7mm, F.Cu at (144.8, 95.6)
- added REF**: VIA_0.7mm, VIA_0.7mm, F.Cu at (130.1, 77.0)
- added REF**: VIA_0.7mm, VIA_0.7mm, F.Cu at (130.1, 75.4)
- added REF**: VIA_0.7mm, VIA_0.7mm, F.Cu at (130.1, 73.8)
- added REF**: VIA_0.7mm, VIA_0.7mm, F.Cu at (130.1, 72.2)
- added REF**: VIA_0.7mm, VIA_0.7mm, F.Cu at (155.1, 80.2)
- added REF**: VIA_0.7mm, VIA_0.7mm, F.Cu at (155.1, 78.6)
- added REF**: VIA_0.7mm, VIA_0.7mm, F.Cu at (155.1, 77.0)
- added REF**: VIA_0.7mm, VIA_0.7mm, F.Cu at (155.1, 75.4)
- added REF**: VIA_0.7mm, VIA_0.7mm, F.Cu at (155.1, 73.8)
- added REF**: VIA_0.7mm, VIA_0.7mm, F.Cu at (105.1, 80.2)
- added REF**: VIA_0.7mm, VIA_0.7mm, F.Cu at (116.6, 98.8)
- added REF**: VIA_0.7mm, VIA_0.7mm, F.Cu at (143.2, 95.6)
- added REF**: VIA_0.7mm, VIA_0.7mm, F.Cu at (105.1, 78.6)
- added REF**: VIA_0.7mm, VIA_0.7mm, F.Cu at (105.1, 77.0)
- added REF**: VIA_0.7mm, VIA_0.7mm, F.Cu at (105.1, 75.4)
- added REF**: VIA_0.7mm, VIA_0.7mm, F.Cu at (105.1, 73.8)
- added REF**: VIA_0.7mm, VIA_0.7mm, F.Cu at (105.1, 72.2)
- added REF**: VIA_0.7mm, VIA_0.7mm, F.Cu at (158.4, 92.3)
- added REF**: VIA_0.7mm, VIA_0.7mm, F.Cu at (157.0, 92.3)
- added REF**: VIA_0.7mm, VIA_0.7mm, F.Cu at (155.6, 92.3)
- added REF**: VIA_0.7mm, VIA_0.7mm, F.Cu at (158.4, 90.9)
- added REF**: VIA_0.7mm, VIA_0.7mm, F.Cu at (157.0, 90.9)
- added REF**: VIA_0.7mm, VIA_0.7mm, F.Cu at (141.6, 95.6)
- added REF**: VIA_0.7mm, VIA_0.7mm, F.Cu at (170.2, 102.9)
- added REF**: VIA_0.7mm, VIA_0.7mm, F.Cu at (168.8, 102.9)
- added REF**: VIA_0.7mm, VIA_0.7mm, F.Cu at (170.2, 101.5)
- added REF**: VIA_0.7mm, VIA_0.7mm, F.Cu at (168.8, 101.5)
- added REF**: VIA_0.7mm, VIA_0.7mm, F.Cu at (170.2, 100.1)
- added REF**: VIA_0.7mm, VIA_0.7mm, F.Cu at (154.2, 97.0)
- added REF**: VIA_0.7mm, VIA_0.7mm, F.Cu at (152.8, 97.0)
- added REF**: VIA_0.7mm, VIA_0.7mm, F.Cu at (154.2, 95.6)
- added REF**: VIA_0.7mm, VIA_0.7mm, F.Cu at (152.8, 95.6)
- added REF**: VIA_0.7mm, VIA_0.7mm, F.Cu at (154.2, 94.2)
- added REF**: VIA_0.7mm, VIA_0.7mm, F.Cu at (143.2, 94.0)
- added REF**: VIA_0.7mm, VIA_0.7mm, F.Cu at (145.2, 102.9)
- added REF**: VIA_0.7mm, VIA_0.7mm, F.Cu at (143.8, 102.9)
- added REF**: VIA_0.7mm, VIA_0.7mm, F.Cu at (145.2, 101.5)
- added REF**: VIA_0.7mm, VIA_0.7mm, F.Cu at (143.8, 101.5)
- added REF**: VIA_0.7mm, VIA_0.7mm, F.Cu at (145.2, 100.1)
- added REF**: VIA_0.7mm, VIA_0.7mm, F.Cu at (129.2, 97.0)
- added REF**: VIA_0.7mm, VIA_0.7mm, F.Cu at (127.8, 97.0)
- added REF**: VIA_0.7mm, VIA_0.7mm, F.Cu at (129.2, 95.6)
- added REF**: VIA_0.7mm, VIA_0.7mm, F.Cu at (127.8, 95.6)
- added REF**: VIA_0.7mm, VIA_0.7mm, F.Cu at (129.2, 94.2)
- added REF**: VIA_0.7mm, VIA_0.7mm, F.Cu at (141.6, 94.0)
- added REF**: VIA_0.7mm, VIA_0.7mm, F.Cu at (133.4, 92.3)
- added REF**: VIA_0.7mm, VIA_0.7mm, F.Cu at (132.0, 92.3)
- added REF**: VIA_0.7mm, VIA_0.7mm, F.Cu at (130.6, 92.3)
- added REF**: VIA_0.7mm, VIA_0.7mm, F.Cu at (133.4, 90.9)
- added REF**: VIA_0.7mm, VIA_0.7mm, F.Cu at (132.0, 90.9)
- added REF**: VIA_0.7mm, VIA_0.7mm, F.Cu at (104.2, 97.0)
- added REF**: VIA_0.7mm, VIA_0.7mm, F.Cu at (102.8, 97.0)
- added REF**: VIA_0.7mm, VIA_0.7mm, F.Cu at (104.2, 95.6)
- added REF**: VIA_0.7mm, VIA_0.7mm, F.Cu at (102.8, 95.6)
- added REF**: VIA_0.7mm, VIA_0.7mm, F.Cu at (104.2, 94.2)
- added REF**: VIA_0.7mm, VIA_0.7mm, F.Cu at (191.6, 92.4)
- added REF**: VIA_0.7mm, VIA_0.7mm, F.Cu at (108.4, 92.3)
- added REF**: VIA_0.7mm, VIA_0.7mm, F.Cu at (107.0, 92.3)
- added REF**: VIA_0.7mm, VIA_0.7mm, F.Cu at (105.6, 92.3)
- added REF**: VIA_0.7mm, VIA_0.7mm, F.Cu at (108.4, 90.9)
- added REF**: VIA_0.7mm, VIA_0.7mm, F.Cu at (107.0, 90.9)
- added REF**: VIA_0.7mm, VIA_0.7mm, F.Cu at (155.6, 90.9)
- added REF**: VIA_0.7mm, VIA_0.7mm, F.Cu at (130.6, 90.9)
- added REF**: VIA_0.7mm, VIA_0.7mm, F.Cu at (105.6, 90.9)
- added REF**: VIA_0.7mm, VIA_0.7mm, F.Cu at (152.8, 94.2)
- added REF**: VIA_0.7mm, VIA_0.7mm, F.Cu at (127.8, 94.2)
- added REF**: VIA_0.7mm, VIA_0.7mm, F.Cu at (166.6, 92.4)
- added REF**: VIA_0.7mm, VIA_0.7mm, F.Cu at (102.8, 94.2)
- added REF**: VIA_0.7mm, VIA_0.7mm, F.Cu at (130.1, 70.6)
- added REF**: VIA_0.7mm, VIA_0.7mm, F.Cu at (105.1, 70.6)
- added REF**: VIA_0.7mm, VIA_0.7mm, F.Cu at (168.8, 100.1)
- added REF**: VIA_0.7mm, VIA_0.7mm, F.Cu at (143.8, 100.1)
- added REF**: VIA_0.7mm, VIA_0.7mm, F.Cu at (118.8, 100.1)
- added REF**: VIA_0.7mm, VIA_0.7mm, F.Cu at (171.2, 90.8)
- added REF**: VIA_0.7mm, VIA_0.7mm, F.Cu at (146.2, 90.8)
- added REF**: VIA_0.7mm, VIA_0.7mm, F.Cu at (121.2, 90.8)
- added REF**: VIA_0.7mm, VIA_0.7mm, F.Cu at (199.4, 98.8)
- added REF**: VIA_0.7mm, VIA_0.7mm, F.Cu at (141.6, 92.4)
- added REF**: VIA_0.7mm, VIA_0.7mm, F.Cu at (194.8, 98.8)
- added REF**: VIA_0.7mm, VIA_0.7mm, F.Cu at (193.2, 98.8)
- added REF**: VIA_0.7mm, VIA_0.7mm, F.Cu at (191.6, 98.8)
- added REF**: VIA_0.7mm, VIA_0.7mm, F.Cu at (199.4, 97.2)
- added REF**: VIA_0.7mm, VIA_0.7mm, F.Cu at (194.8, 97.2)
- added REF**: VIA_0.7mm, VIA_0.7mm, F.Cu at (193.2, 97.2)
- added REF**: VIA_0.7mm, VIA_0.7mm, F.Cu at (191.6, 97.2)
- added REF**: VIA_0.7mm, VIA_0.7mm, F.Cu at (199.4, 95.6)
- added REF**: VIA_0.7mm, VIA_0.7mm, F.Cu at (194.8, 95.6)
- added REF**: VIA_0.7mm, VIA_0.7mm, F.Cu at (193.2, 95.6)
- added REF**: VIA_0.7mm, VIA_0.7mm, F.Cu at (124.4, 103.6)
- added REF**: VIA_0.7mm, VIA_0.7mm, F.Cu at (191.6, 95.6)
- added REF**: VIA_0.7mm, VIA_0.7mm, F.Cu at (199.4, 94.0)
- added REF**: VIA_0.7mm, VIA_0.7mm, F.Cu at (193.2, 94.0)
- added REF**: VIA_0.7mm, VIA_0.7mm, F.Cu at (191.6, 94.0)
- added REF**: VIA_0.7mm, VIA_0.7mm, F.Cu at (199.4, 92.4)
- added REF**: VIA_0.7mm, VIA_0.7mm, F.Cu at (197.8, 92.4)
- added REF**: VIA_0.7mm, VIA_0.7mm, F.Cu at (116.6, 92.4)
- added REF**: VIA_0.7mm, VIA_0.7mm, F.Cu at (199.4, 90.8)
- added REF**: VIA_0.7mm, VIA_0.7mm, F.Cu at (197.8, 90.8)
- added REF**: VIA_0.7mm, VIA_0.7mm, F.Cu at (196.2, 90.8)
- added REF**: VIA_0.7mm, VIA_0.7mm, F.Cu at (124.4, 102.0)
- added REF**: VIA_0.7mm, VIA_0.7mm, F.Cu at (191.1, 84.9)
- added REF**: VIA_0.7mm, VIA_0.7mm, F.Cu at (184.9, 80.3)
- added REF**: VIA_0.7mm, VIA_0.7mm, F.Cu at (196.1, 89.8)
- added REF**: VIA_0.7mm, VIA_0.7mm, F.Cu at (194.5, 89.8)
- added REF**: VIA_0.7mm, VIA_0.7mm, F.Cu at (192.9, 89.8)
- added REF**: VIA_0.7mm, VIA_0.7mm, F.Cu at (191.3, 89.8)
- added REF**: VIA_0.7mm, VIA_0.7mm, F.Cu at (189.7, 89.8)
- added REF**: VIA_0.7mm, VIA_0.7mm, F.Cu at (188.1, 89.8)
- added REF**: VIA_0.7mm, VIA_0.7mm, F.Cu at (186.5, 89.7)
- added REF**: VIA_0.7mm, VIA_0.7mm, F.Cu at (184.9, 89.7)
- added REF**: VIA_0.7mm, VIA_0.7mm, F.Cu at (124.4, 100.4)
- added REF**: VIA_0.7mm, VIA_0.7mm, F.Cu at (183.3, 89.8)
- added REF**: VIA_0.7mm, VIA_0.7mm, F.Cu at (181.7, 89.8)
- added REF**: VIA_0.7mm, VIA_0.7mm, F.Cu at (180.1, 89.8)
- added REF**: VIA_0.7mm, VIA_0.7mm, F.Cu at (196.1, 88.2)
- added REF**: VIA_0.7mm, VIA_0.7mm, F.Cu at (194.5, 88.2)
- added REF**: VIA_0.7mm, VIA_0.7mm, F.Cu at (192.9, 88.2)
- added REF**: VIA_0.7mm, VIA_0.7mm, F.Cu at (191.3, 88.2)
- added REF**: VIA_0.7mm, VIA_0.7mm, F.Cu at (189.7, 88.2)
- added REF**: VIA_0.7mm, VIA_0.7mm, F.Cu at (188.1, 88.2)
- added REF**: VIA_0.7mm, VIA_0.7mm, F.Cu at (186.5, 88.2)
- added REF**: VIA_0.7mm, VIA_0.7mm, F.Cu at (119.8, 97.2)
- added REF**: VIA_0.7mm, VIA_0.7mm, F.Cu at (149.4, 103.6)
- added REF**: VIA_0.7mm, VIA_0.7mm, F.Cu at (184.9, 88.2)
- added REF**: VIA_0.7mm, VIA_0.7mm, F.Cu at (183.3, 88.2)
- added REF**: VIA_0.7mm, VIA_0.7mm, F.Cu at (181.7, 88.2)
- added REF**: VIA_0.7mm, VIA_0.7mm, F.Cu at (180.1, 88.2)
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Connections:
- net Net-(C17-Pad1) renamed /Output_2/6V_Regulator/BYPASS
- net Net-(C26-Pad1) renamed /Output_3/6V_Regulator/BYPASS
- net Net-(C35-Pad1) renamed /Output_4/6V_Regulator/BYPASS
- net Net-(C44-Pad1) renamed /Output_1/6V_Regulator/BYPASS
- net Net-(D1-Pad2) renamed /Output_2/REV_ON
- net Net-(D10-Pad2) renamed /Output_1/REV_ON
- net Net-(D4-Pad2) renamed /Output_3/REV_ON
- net Net-(D7-Pad2) renamed /Output_4/REV_ON
- C11 pad 2: /Output_2/PWRGND -> /Output_2/GNDSUPPLY
- C13 pad 2: /Output_2/PWRGND -> /Output_2/GNDSUPPLY
- C14 pad 2: /Output_2/PWRGND -> /Output_2/GNDSUPPLY
- C15 pad 2: /Output_2/PWRGND -> /Output_2/GNDSUPPLY
- C16 pad 2: /Output_2/PWRGND -> /Output_2/GNDSUPPLY
- C17 pad 2: /Output_2/PWRGND -> /Output_2/GNDSUPPLY
- C18 pad 2: /Output_3/PWRGND -> /Output_3/GNDSUPPLY
- C20 pad 2: /Output_3/PWRGND -> /Output_3/GNDSUPPLY
- C22 pad 2: /Output_3/PWRGND -> /Output_3/GNDSUPPLY
- C23 pad 2: /Output_3/PWRGND -> /Output_3/GNDSUPPLY
- C24 pad 2: /Output_3/PWRGND -> /Output_3/GNDSUPPLY
- C25 pad 2: /Output_3/PWRGND -> /Output_3/GNDSUPPLY
- C26 pad 2: /Output_3/PWRGND -> /Output_3/GNDSUPPLY
- C27 pad 2: /Output_4/PWRGND -> /Output_4/GNDSUPPLY
- C29 pad 2: /Output_4/PWRGND -> /Output_4/GNDSUPPLY
- C31 pad 2: /Output_4/PWRGND -> /Output_4/GNDSUPPLY
- C32 pad 2: /Output_4/PWRGND -> /Output_4/GNDSUPPLY
- C33 pad 2: /Output_4/PWRGND -> /Output_4/GNDSUPPLY
- C34 pad 2: /Output_4/PWRGND -> /Output_4/GNDSUPPLY
- C35 pad 2: /Output_4/PWRGND -> /Output_4/GNDSUPPLY
- C36 pad 2: /Output_1/PWRGND -> /Output_1/GNDSUPPLY
- C38 pad 2: /Output_1/PWRGND -> /Output_1/GNDSUPPLY
- C40 pad 2: /Output_1/PWRGND -> /Output_1/GNDSUPPLY
- C41 pad 2: /Output_1/PWRGND -> /Output_1/GNDSUPPLY
- C42 pad 2: /Output_1/PWRGND -> /Output_1/GNDSUPPLY
- C43 pad 2: /Output_1/PWRGND -> /Output_1/GNDSUPPLY
- C44 pad 2: /Output_1/PWRGND -> /Output_1/GNDSUPPLY
- C9 pad 2: /Output_2/PWRGND -> /Output_2/GNDSUPPLY
- D11 pad 1: /Output_1/PWRGND -> /Output_1/GNDSUPPLY
- D11 pad 2: Net-(D11-Pad2) -> /Output_1/LED_LIM
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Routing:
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- added copper zone on B.Cu, net /Output_1/GNDSUPPLY
- added copper zone on F.Cu, net /Output_1/GNDSUPPLY
- added copper zone on B.Cu, net /Output_1/V5
- added copper zone on F.Cu, net /Output_1/V5
- added copper zone on B.Cu, net /Output_1/V_PROTECTED
- added copper zone on F.Cu, net /Output_1/V_PROTECTED
- added copper zone on B.Cu, net /Output_2/GNDSUPPLY
- added copper zone on F.Cu, net /Output_2/GNDSUPPLY
- added copper zone on B.Cu, net /Output_2/V5
- added copper zone on F.Cu, net /Output_2/V5
- added copper zone on B.Cu, net /Output_2/V_PROTECTED
- added copper zone on F.Cu, net /Output_2/V_PROTECTED
- added copper zone on B.Cu, net /Output_3/GNDSUPPLY
- added copper zone on F.Cu, net /Output_3/GNDSUPPLY
- added copper zone on B.Cu, net /Output_3/V5
- added copper zone on F.Cu, net /Output_3/V5
- added copper zone on B.Cu, net /Output_3/V_PROTECTED
- added copper zone on F.Cu, net /Output_3/V_PROTECTED
- added copper zone on B.Cu, net /Output_4/GNDSUPPLY
- added copper zone on F.Cu, net /Output_4/GNDSUPPLY
- added copper zone on B.Cu, net /Output_4/V5
- added copper zone on F.Cu, net /Output_4/V5
- added copper zone on B.Cu, net /Output_4/V_PROTECTED
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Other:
- net class LowPower: trace_width 0.7 -> 0.5
